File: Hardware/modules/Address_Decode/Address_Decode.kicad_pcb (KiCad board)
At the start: 4 copper layers, 83.3 x 68.2 mm, 33 parts, among them J1 Bus_PCI_6502, J2 Clock_Sel, J3 Conn_01x08, SW1 Manual_Clock, U1 74HC14, U2 74HC00, U3 74LS20, U4 DS1501YZ, U5 74LS393, U6 74HC138, U7 74HC688, X1 8MHz, Y1 G33270007

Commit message: Big Hardware Update
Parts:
- moved Ref** 52.7 mm to (133.0, 87.0), turned to 90 degrees
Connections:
- U2 pad 9: /PORT_160 -> /PORT_144
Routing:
- net /PORT_160: track 35.2 -> 4.35 mm
- net /PORT_144: track 4.35 -> 34.5 mm
- net GND: track 48.1 -> 50.9 mm, vias 42 -> 43
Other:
- board text added: "$BF90 - $BF9F"
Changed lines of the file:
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@@
 			(layers "*.Cu" "*.Mask")
 			(remove_unused_layers no)
-			(net 90 "/PORT_160")
+			(net 94 "/PORT_144")
 			(pintype "input")
 		)
@@
 	(footprint "Eigene:ladder_4"
 		(layer "F.Cu")
-		(at 144.526 35.56)
+		(at 132.969 86.995 90)
 		(property "Reference" "Ref**"
-			(at 0 0 0)
+			(at 0 0 90)
 			(layer "F.SilkS")
 			(hide yes)
@@
 		)
 		(property "Value" "Val**"
-			(at 0 0 0)
+			(at 0 0 90)
 			(layer "F.SilkS")
 			(hide yes)
@@
 		)
 		(property "Footprint" "Eigene:ladder_4"
-			(at 0 0 0)
+			(at 0 0 90)
 			(layer "F.Fab")
 			(hide yes)
@@
 		)
 		(property "Datasheet" ""
-			(at 0 0 0)
+			(at 0 0 90)
 			(layer "F.Fab")
 			(hide yes)
@@
 		)
 		(property "Description" ""
-			(at 0 0 0)
+			(at 0 0 90)
 			(layer "F.Fab")
 			(hide yes)
@@
 		(attr smd)
 		(fp_line
-			(start -2.54 -1.27)
-			(end -2.54 1.27)
+			(start 2.54 -1.27)
+			(end 2.54 1.27)
 			(stroke
 				(width 0.2)
@@
 		)
 		(fp_line
-			(start 2.54 -1.27)
-			(end 2.54 1.27)
+			(start -2.54 -1.27)
+			(end -2.54 1.27)
 			(stroke
 				(width 0.2)
@@
 		)
 		(fp_line
-			(start -2.54 -1.27)
-			(end -2.54 1.27)
+			(start 2.54 -1.27)
+			(end 2.54 1.27)
 			(stroke
 				(width 0.2)
@@
 		)
 		(fp_line
-			(start 2.54 -1.27)
-			(end 2.54 1.27)
+			(start -2.54 -1.27)
+			(end -2.54 1.27)
 			(stroke
 				(width 0.2)
@@
 		)
 		(fp_line
-			(start -2.54 -1.27)
-			(end -2.54 1.27)
+			(start 2.54 -1.27)
+			(end 2.54 1.27)
 			(stroke
 				(width 0.2)
@@
 		)
 		(fp_line
-			(start 2.54 -1.27)
-			(end 2.54 1.27)
+			(start -2.54 -1.27)
+			(end -2.54 1.27)
 			(stroke
 				(width 0.2)
@@
 		)
 		(fp_line
-			(start -2.54 -1.27)
-			(end -2.54 1.27)
+			(start 2.54 -1.27)
+			(end 2.54 1.27)
 			(stroke
 				(width 0.2)
@@
 		)
 		(fp_line
-			(start 2.54 -1.27)
-			(end 2.54 1.27)
+			(start -2.54 -1.27)
+			(end -2.54 1.27)
 			(stroke
 				(width 0.2)
@@
 		)
 		(fp_text user "1"
-			(at -3.81 0 0)
+			(at -3.81 0 90)
 			(layer "F.Cu")
 			(effects
@@
 		)
 		(fp_text user "2"
-			(at -1.27 0 0)
+			(at -1.27 0 90)
 			(layer "In1.Cu")
 			(effects
@@
 		)
 		(fp_text user "3"
-			(at 1.27 0 0)
+			(at 1.27 0 90)
 			(layer "In2.Cu")
 			(effects
@@
 		)
 		(fp_text user "4"
-			(at 3.81 0 0)
+			(at 3.81 0 90)
 			(layer "B.Cu")
 			(effects
@@
 		)
 	)
+	(gr_text "$BF90 - $BF9F"
+		(at 182.118 92.837 0)
+		(layer "F.SilkS")
+		(effects
+			(font
+				(size 1 1)
+				(thickness 0.2)
+				(bold yes)
+			)
+			(justify left bottom)
+		)
+	)
 	(gr_text "1M"
 		(at 191.008 42.926 90)
@@
 	)
 	(segment
+		(start 153.279 94.117)
+		(end 153.289 94.107)
+		(width 0.25)
+		(layer "F.Cu")
+		(net 2)
+	)
+	(segment
 		(start 207.325 89.027)
 		(end 208.534 89.027)
@@
 		(net 2)
 	)
+	(segment
+		(start 153.279 96.901)
+		(end 153.279 94.117)
+		(width 0.25)
+		(layer "F.Cu")
+		(net 2)
+	)
 	(via
 		(at 195.199 99.568)
@@
 	)
 	(via
+		(at 153.289 94.107)
+		(size 0.46)
+		(drill 0.2)
+		(layers "F.Cu" "B.Cu")
+		(net 2)
+	)
+	(via
 		(at 157.353 82.042)
 		(size 0.46)
@@
 	)
 	(segment
-		(start 196.977 58.801)
-		(end 191.77 58.801)
-		(width 0.3)
-		(layer "B.Cu")
-		(net 90)
-	)
-	(segment
-		(start 173.736 65.913)
-		(end 172.72 66.929)
-		(width 0.3)
-		(layer "B.Cu")
-		(net 90)
-	)
-	(segment
-		(start 201.549 54.991)
-		(end 200.787 54.991)
-		(width 0.3)
-		(layer "B.Cu")
-		(net 90)
-	)
-	(segment
-		(start 198.247 57.531)
-		(end 196.977 58.801)
-		(width 0.3)
-		(layer "B.Cu")
-		(net 90)
-	)
-	(segment
-		(start 182.372 61.341)
-		(end 177.8 65.913)
-		(width 0.3)
-		(layer "B.Cu")
-		(net 90)
-	)
-	(segment
-		(start 172.72 66.929)
-		(end 172.72 68.3223)
-		(width 0.3)
-		(layer "B.Cu")
-		(net 90)
-	)
-	(segment
-		(start 177.8 65.913)
-		(end 173.736 65.913)
-		(width 0.3)
-		(layer "B.Cu")
-		(net 90)
-	)
-	(segment
 		(start 200.787 54.991)
 		(end 198.247 57.531)
-		(width 0.3)
+		(width 0.25)
 		(layer "B.Cu")
 		(net 90)
 	)
 	(segment
-		(start 189.23 61.341)
-		(end 182.372 61.341)
-		(width 0.3)
-		(layer "B.Cu")
-		(net 90)
-	)
-	(segment
-		(start 191.77 58.801)
-		(end 189.23 61.341)
-		(width 0.3)
+		(start 201.549 54.991)
+		(end 200.787 54.991)
+		(width 0.25)
 		(layer "B.Cu")
 		(net 90)
@@
 	)
 	(segment
+		(start 178.562 65.532)
+		(end 173.482 65.532)
+		(width 0.25)
+		(layer "B.Cu")
+		(net 94)
+	)
+	(segment
+		(start 173.482 65.532)
+		(end 172.72 66.294)
+		(width 0.25)
+		(layer "B.Cu")
+		(net 94)
+	)
+	(segment
+		(start 182.753 61.341)
+		(end 178.562 65.532)
+		(width 0.25)
+		(layer "B.Cu")
+		(net 94)
+	)
+	(segment
 		(start 201.549 57.531)
 		(end 200.787 57.531)
@@
 		(layer "B.Cu")
 		(net 94)
+	)
+	(segment
+		(start 172.72 66.294)
+		(end 172.72 68.3223)
+		(width 0.25)
+		(layer "B.Cu")
+		(net 94)
+	)
+	(segment
+		(start 198.247 60.071)
+		(end 196.977 61.341)
+		(width 0.25)
+		(layer "B.Cu")
+		(net 94)
+	)
+	(segment
+		(start 196.977 61.341)
+		(end 182.753 61.341)
+		(width 0.25)
+		(layer "B.Cu")
+		(net 94)

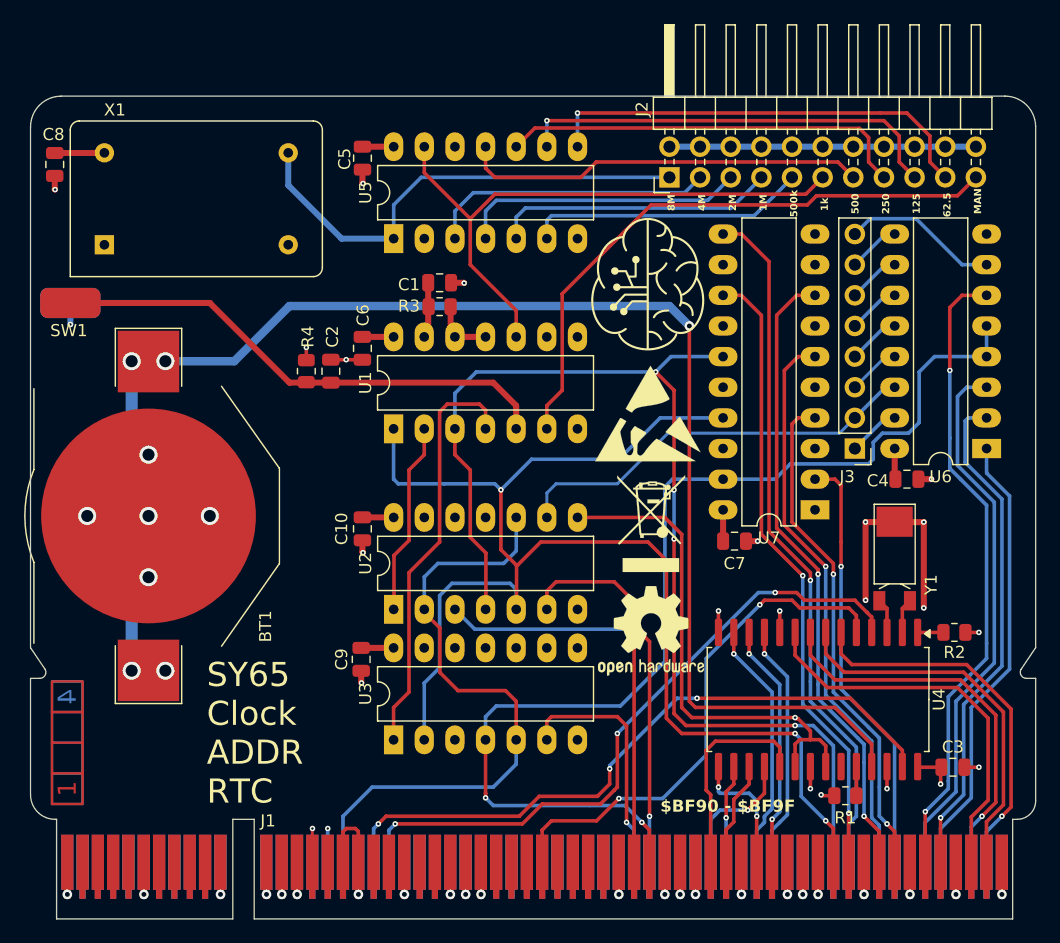
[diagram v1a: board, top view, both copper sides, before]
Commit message: Hardware Update Add MyCPU VGA Module Beautify all Schematics minor Error corrections Readme Update
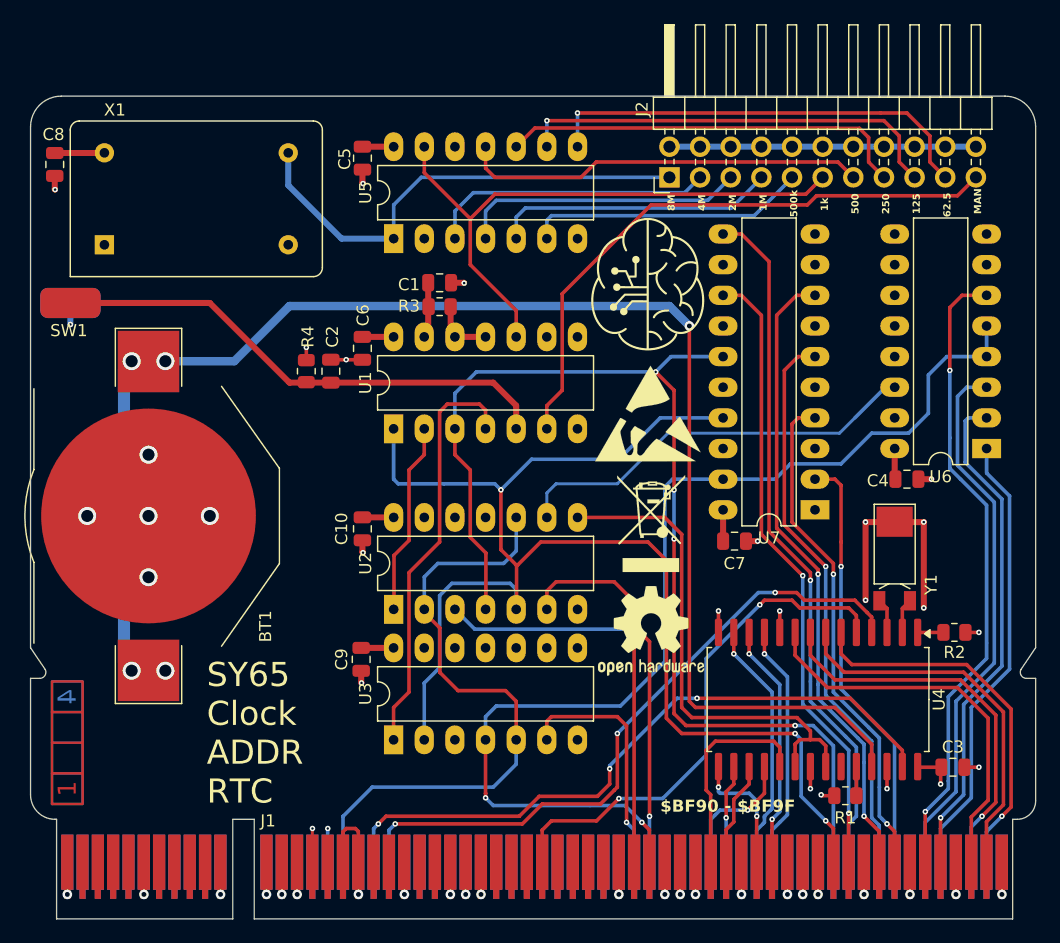
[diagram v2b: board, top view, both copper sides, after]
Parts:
- removed J3: Conn_01x08, Connector_PinHeader_2.54mm:PinHeader_1x08_P2.54mm_Vertical
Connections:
- J1 pad A27: /~{IRQ_0.0} -> unconnected-(J1-~{IRQ_0.0}-PadA27)
- J1 pad A28: /~{IRQ_0.1} -> unconnected-(J1-~{IRQ_0.1}-PadA28)
- J1 pad A29: /~{IRQ_0.2} -> unconnected-(J1-~{IRQ_0.2}-PadA29)
- J1 pad A30: /~{IRQ_0.3} -> unconnected-(J1-~{IRQ_0.3}-PadA30)
- J1 pad A32: /~{IRQ_0.5} -> unconnected-(J1-~{IRQ_0.5}-PadA32)
- J1 pad A33: /~{IRQ_0.6} -> unconnected-(J1-~{IRQ_0.6}-PadA33)
- J1 pad A34: /~{IRQ_0.7} -> unconnected-(J1-~{IRQ_0.7}-PadA34)
- J1 pad A38: /SYNC_VPA -> unconnected-(J1-Sync/VPA-PadA38)
- J1 pad A39: /Ø2/VDA -> unconnected-(J1-Ø2/VDA-PadA39)
- J1 pad A41: /~{RDY} -> unconnected-(J1-~{RDY}-PadA41)
- J1 pad A42: /~{BE} -> unconnected-(J1-~{BE}-PadA42)
- J1 pad A45: /E -> unconnected-(J1-E-PadA45)
- J1 pad A53: /RAM_0 -> unconnected-(J1-RAM0-PadA53)
- J1 pad A54: /RAM_1 -> unconnected-(J1-RAM1-PadA54)
- J1 pad A55: /RAM_2 -> unconnected-(J1-RAM2-PadA55)
- J1 pad A56: /RAM_3 -> unconnected-(J1-RAM3-PadA56)
- J1 pad A58: /RAM_4 -> unconnected-(J1-RAM4-PadA58)
- J1 pad A59: /RAM_5 -> unconnected-(J1-RAM5-PadA59)
- J1 pad A60: /RAM_6 -> unconnected-(J1-RAM6-PadA60)
- J1 pad A61: /RAM_7 -> unconnected-(J1-RAM7-PadA61)
- J1 pad B27: /~{IRQ} -> unconnected-(J1-~{IRQ}-PadB27)
- J1 pad B28: /~{IRQ_0} -> unconnected-(J1-~{IRQ_0}-PadB28)
- J1 pad B29: /~{IRQ_1} -> unconnected-(J1-~{IRQ_1}-PadB29)
- J1 pad B30: /~{IRQ_2} -> unconnected-(J1-~{IRQ_2}-PadB30)
- J1 pad B31: /~{IRQ_3} -> unconnected-(J1-~{IRQ_3}-PadB31)
- J1 pad B32: /~{IRQ_4} -> unconnected-(J1-~{IRQ_4}-PadB32)
- J1 pad B33: /~{NMI} -> unconnected-(J1-~{NMI}-PadB33)
- J1 pad B34: /PAGE -> unconnected-(J1-PAGE_ROM-PadB34)
- J1 pad B38: /~{VP} -> unconnected-(J1-~{VP}-PadB38)
- J1 pad B39: /~{ML} -> unconnected-(J1-~{ML}-PadB39)
- J1 pad B46: /M/X -> unconnected-(J1-M/~{X}-PadB46)
- J1 pad B53: /ROM_0 -> unconnected-(J1-ROM0-PadB53)
- J1 pad B54: /ROM_1 -> unconnected-(J1-ROM1-PadB54)
- J1 pad B55: /ROM_2 -> unconnected-(J1-ROM2-PadB55)
- J1 pad B56: /ROM_3 -> unconnected-(J1-ROM3-PadB56)
- J1 pad B58: /ROM_4 -> unconnected-(J1-ROM4-PadB58)
- J1 pad B59: /ROM_5 -> unconnected-(J1-ROM5-PadB59)
- J1 pad B60: /ROM_6 -> unconnected-(J1-ROM6-PadB60)
- J1 pad B61: /ROM_7 -> unconnected-(J1-ROM7-PadB61)
- U6 pad 10: /PORT_208 -> unconnected-(U6-~{Y5}-Pad10)
- U6 pad 11: /PORT_192 -> unconnected-(U6-~{Y4}-Pad11)
- U6 pad 12: /PORT_176 -> unconnected-(U6-~{Y3}-Pad12)
- U6 pad 13: /PORT_160 -> unconnected-(U6-~{Y2}-Pad13)
- U6 pad 15: /PORT_128 -> unconnected-(U6-~{Y0}-Pad15)
- U6 pad 7: /PORT_240 -> unconnected-(U6-~{Y7}-Pad7)
- U6 pad 9: /PORT_224 -> unconnected-(U6-~{Y6}-Pad9)
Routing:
- net /PORT_240: track 13.0 -> 0.00 mm
- net /PORT_224: track 4.35 -> 0.00 mm
- net /PORT_208: track 4.35 -> 0.00 mm
- net /PORT_192: track 4.35 -> 0.00 mm
- net /PORT_176: track 4.35 -> 0.00 mm
- net /PORT_160: track 4.35 -> 0.00 mm
- net /PORT_128: track 4.35 -> 0.00 mm
- net /~{IO}: track 92.3 -> 90.9 mm
- net unconnected-(U6-~{Y6}-Pad9): track 0.00 -> 0.76 mm
- net unconnected-(U6-~{Y5}-Pad10): track 0.00 -> 0.76 mm
- net unconnected-(U6-~{Y4}-Pad11): track 0.00 -> 0.76 mm
- net unconnected-(U6-~{Y3}-Pad12): track 0.00 -> 0.76 mm
- net unconnected-(U6-~{Y2}-Pad13): track 0.00 -> 0.76 mm
- net unconnected-(U6-~{Y0}-Pad15): track 0.00 -> 0.76 mm
- net Net-(BT1-+): track 126.8 -> 127.3 mm
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
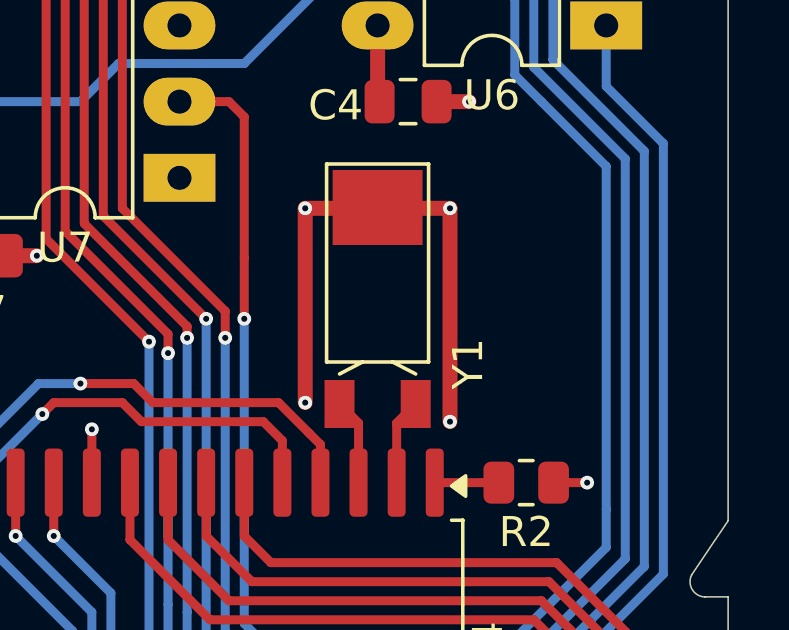
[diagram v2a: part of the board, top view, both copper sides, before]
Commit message: add local ground plane on 32kHz crystal
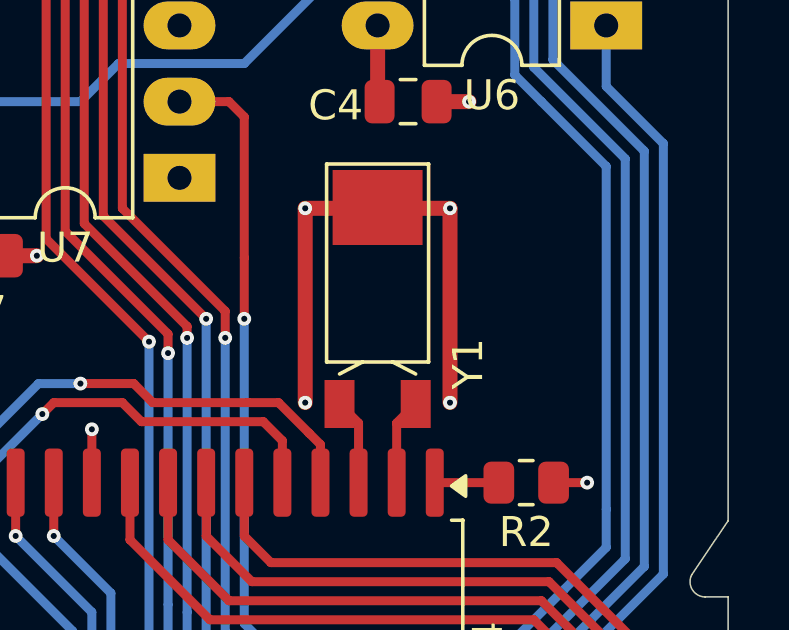
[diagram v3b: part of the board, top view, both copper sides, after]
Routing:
- net GND: track 50.9 -> 50.3 mm
- added copper zone on In1.Cu, net GND
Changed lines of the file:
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@@
 	)
 	(segment
-		(start 203.962 75.819)
-		(end 203.962 68.707)
-		(width 0.5)
-		(layer "F.Cu")
-		(net 2)
-	)
-	(segment
 		(start 156.088 55.25)
 		(end 157.424 55.25)
@@
 	)
 	(segment
+		(start 203.962 75.184)
+		(end 203.962 68.707)
+		(width 0.5)
+		(layer "F.Cu")
+		(net 2)
+	)
+	(segment
 		(start 157.3276 82.0166)
 		(end 157.353 82.042)
@@
 	)
 	(via
-		(at 203.962 75.819)
+		(at 203.962 75.184)
 		(size 0.46)
 		(drill 0.2)
@@
 		(priority 1)
 		(connect_pads
-			(clearance 0.5)
+			(clearance 0.25)
 		)
 		(min_thickness 0.25)
@@
 		(polygon
 			(pts
-				(xy 213.233 100.203) (xy 129.921 100.076) (xy 129.921 33.401) (xy 213.233 33.401)
+				(xy 213.233 100.33) (xy 129.921 100.33) (xy 129.921 33.401) (xy 213.233 33.401)
+			)
+		)
+	)
+	(zone
+		(net 2)
+		(net_name "GND")
+		(layer "In1.Cu")
+		(hatch edge 0.5)
+		(priority 2)
+		(connect_pads
+			(clearance 0.25)
+		)
+		(min_thickness 0.25)
+		(filled_areas_thickness no)
+		(fill yes
+			(thermal_gap 0.25)
+			(thermal_bridge_width 0.5)
+		)
+		(polygon
+			(pts
+				(xy 191.643 75.692) (xy 191.643 80.264) (xy 202.819 80.264) (xy 202.819 76.962) (xy 204.343 75.438)
+				(xy 204.343 66.675) (xy 198.755 66.675) (xy 198.755 75.438) (xy 200.279 76.962) (xy 200.279 79.248)
+				(xy 192.405 79.248) (xy 192.405 75.692)
 			)
 		)
@@
 		(polygon
 			(pts
-				(xy 213.233 100.203) (xy 129.921 100.076) (xy 129.921 33.401) (xy 213.233 33.401)
+				(xy 213.233 100.33) (xy 129.921 100.33) (xy 129.921 33.401) (xy 213.233 33.401)
 			)
 		)

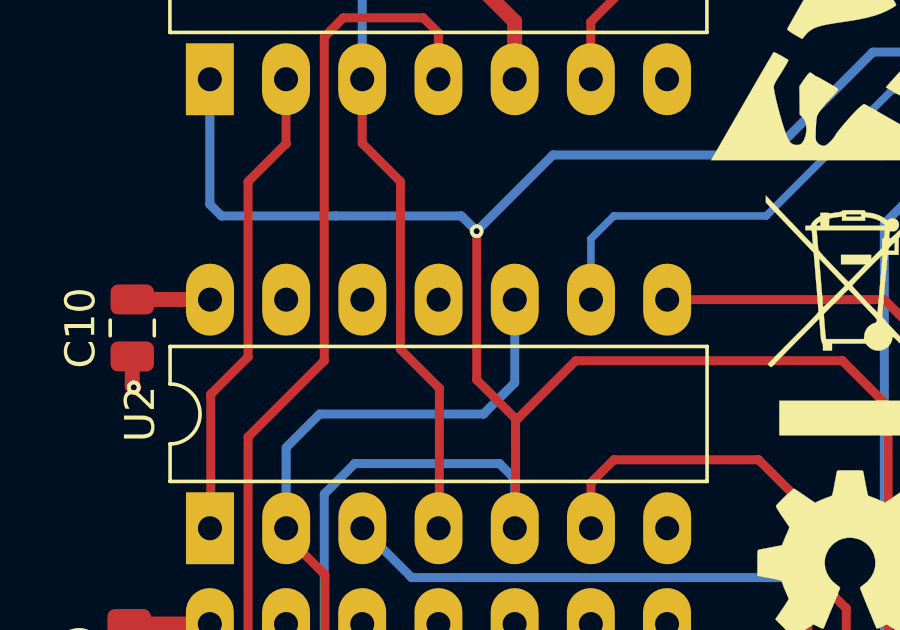
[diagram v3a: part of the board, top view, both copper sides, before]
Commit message: Chip Select Strobe Generation Bugfix
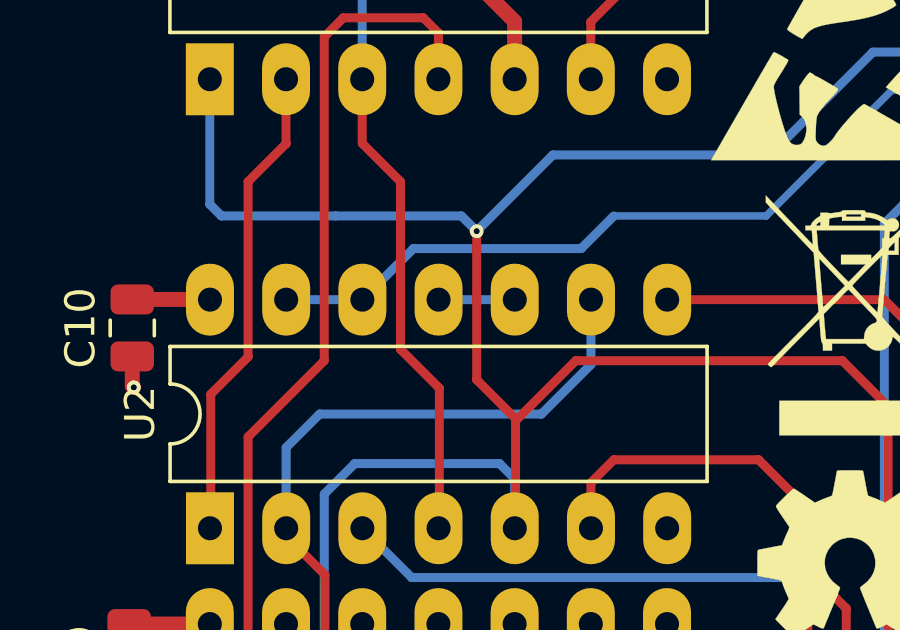
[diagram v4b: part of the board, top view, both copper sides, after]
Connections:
- U2 pad 10: /CLK -> Net-(U2-Pad10)
- U2 pad 11: unconnected-(U2-Pad11) -> Net-(U2-Pad10)
- U2 pad 12: GND -> /PORT_144
- U2 pad 13: GND -> /PORT_144
- U2 pad 9: /PORT_144 -> /CLK
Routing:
- net /PORT_144: track 34.5 -> 43.5 mm
- net Net-(U2-Pad10): track 0.00 -> 2.54 mm
- net /CLK: track 117.5 -> 116.4 mm
